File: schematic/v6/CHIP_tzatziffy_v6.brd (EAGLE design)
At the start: 40.9 x 49.8 mm, 51 parts, among them J1 2X20-CHIP0.8_DRILL, J3 S2B-PH-SM4-TB, Q1 NPN-DTC114YUA, Q2 PNP-DTA114YUA, U1 LMR62421, U3 DS2431P, X1 FH12-40S-0.5SH

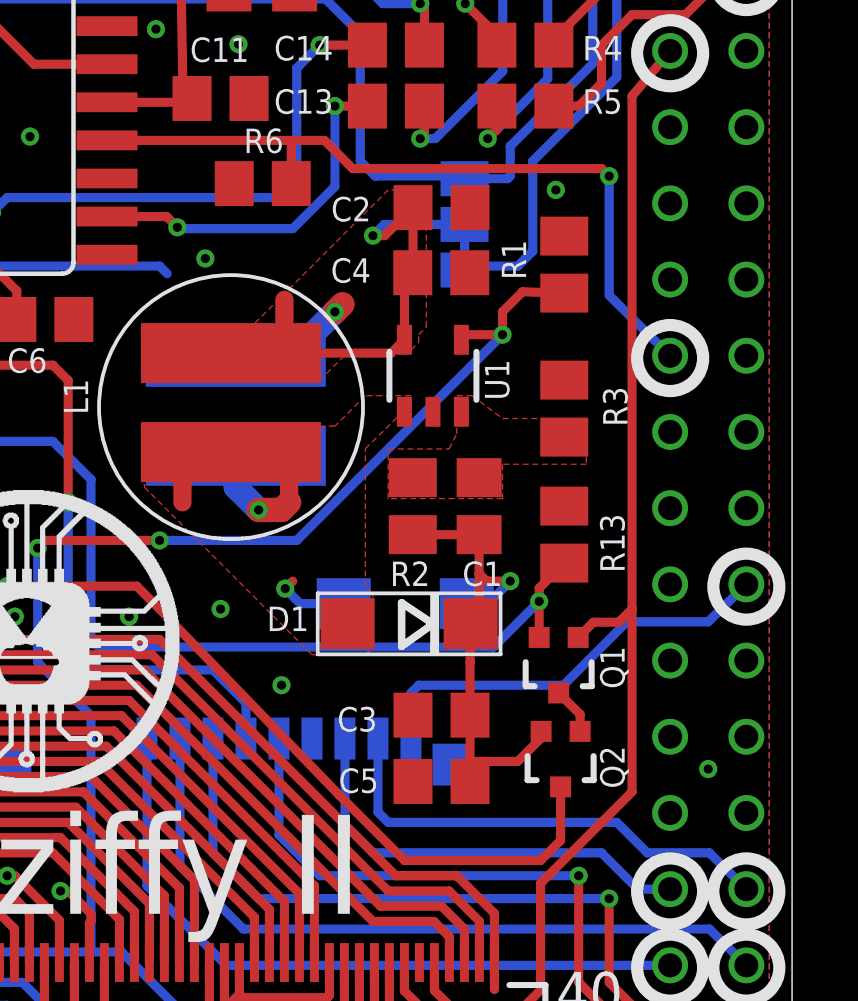
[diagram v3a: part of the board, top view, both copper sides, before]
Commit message: changed 22uF Footprint to 1206
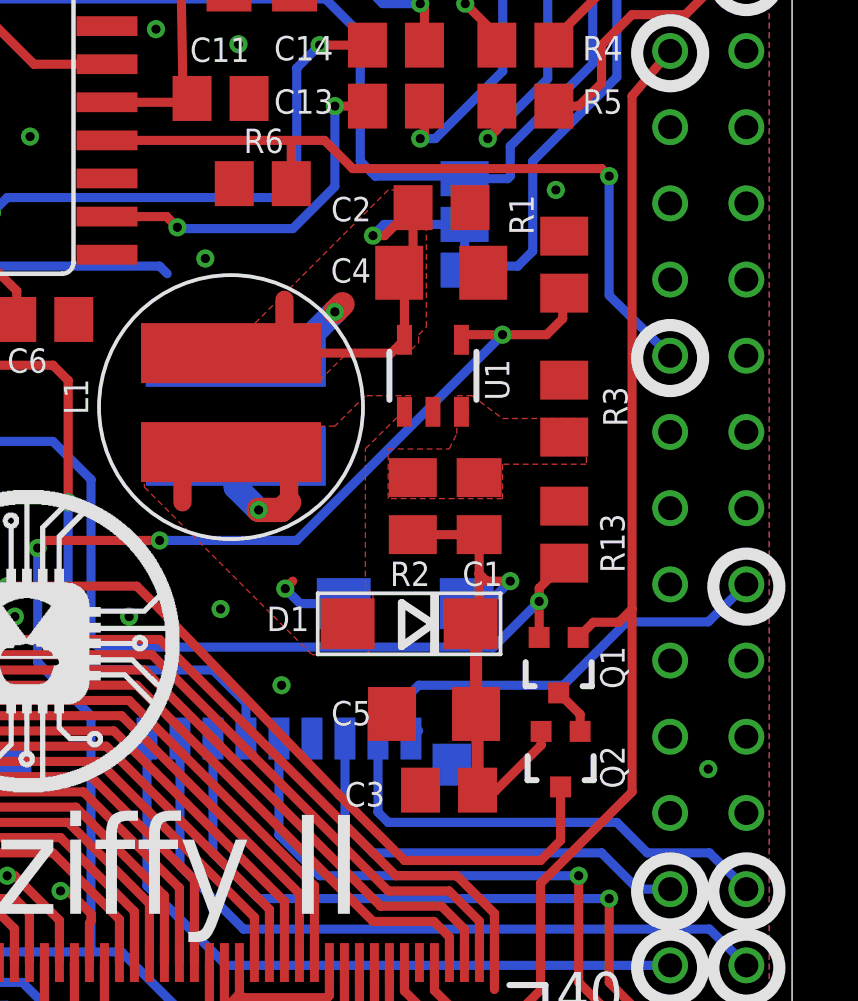
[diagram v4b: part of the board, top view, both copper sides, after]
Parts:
- C4, C5: device rcl:C0805 -> rcl:C1206
- moved C3 2.51 mm to (29.5, 14.3)
- moved C5 2.26 mm to (29.0, 16.8)
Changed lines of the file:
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@@
 </element>
 <element name="R1" library="rcl" package="M0805" value="100K" x="33.3" y="31.8" smashed="yes" rot="R90">
-<attribute name="NAME" x="32.03" y="31.292" size="0.8128" layer="25" rot="R90"/>
+<attribute name="NAME" x="32.28" y="32.792" size="0.8128" layer="25" rot="R90"/>
 <attribute name="VALUE" x="35.84" y="30.53" size="1.27" layer="27" rot="R90"/>
 </element>
@@
 <attribute name="NAME" x="25.527" y="33.2428" size="0.8128" layer="25" font="vector" ratio="12"/>
 </element>
-<element name="C3" library="rcl" package="C0805" value="100nF" x="29.21" y="16.7818" smashed="yes" rot="R180">
-<attribute name="NAME" x="25.7302" y="16.2382" size="0.8128" layer="25" font="vector" ratio="12"/>
-</element>
-<element name="C4" library="rcl" package="C0805" value="22uF" x="29.2" y="31.529" smashed="yes">
+<element name="C3" library="rcl" package="C0805" value="100nF" x="29.46" y="14.2818" smashed="yes" rot="R180">
+<attribute name="NAME" x="25.9802" y="13.7382" size="0.8128" layer="25" font="vector" ratio="12"/>
+</element>
+<element name="C4" library="rcl" package="C1206" value="22uF" x="29.2" y="31.529" smashed="yes">
 <attribute name="NAME" x="25.517" y="31.1988" size="0.8128" layer="25" font="vector" ratio="12"/>
 </element>
-<element name="C5" library="rcl" package="C0805" value="22uF" x="29.21" y="14.572" smashed="yes" rot="R180">
-<attribute name="NAME" x="25.781" y="14.191" size="0.8128" layer="25" font="vector" ratio="12"/>
+<element name="C5" library="rcl" package="C1206" value="22uF" x="28.96" y="16.822" smashed="yes" rot="R180">
+<attribute name="NAME" x="25.531" y="16.441" size="0.8128" layer="25" font="vector" ratio="12"/>
 </element>
 <element name="L1" library="Keyboard v0_5" package="SRN6045" value="SRN6045-100M" x="22.192" y="27.051" smashed="yes" rot="R270">
@@
 <contactref element="D1" pad="C"/>
 <contactref element="Q2" pad="2"/>
-<wire x1="30.16" y1="14.572" x2="30.16" y2="16.7818" width="0.3048" layer="1"/>
-<wire x1="30.16" y1="16.7818" x2="30.16" y2="18.5364" width="0.3048" layer="1"/>
-<wire x1="30.16" y1="18.5364" x2="30.1796" y2="19.826" width="0.3048" layer="1"/>
 <wire x1="29.718" y1="20.2768" x2="29.718" y2="19.558" width="0.3048" layer="1"/>
 <wire x1="29.718" y1="19.558" x2="29.986" y2="19.826" width="0.3048" layer="1"/>
 <wire x1="29.986" y1="19.826" x2="30.1796" y2="19.826" width="0.3048" layer="1"/>
-<wire x1="32.528496875" y1="16.2404625" x2="32.528496875" y2="16.018496875" width="0.3048" layer="1"/>
-<wire x1="32.528496875" y1="16.018496875" x2="31.75" y2="15.24" width="0.3048" layer="1"/>
-<wire x1="31.75" y1="15.24" x2="30.254" y2="15.24" width="0.3048" layer="1"/>
-<wire x1="30.254" y1="15.24" x2="30.16" y2="14.572" width="0.3048" layer="1"/>
 <wire x1="28.2524" y1="22.799" x2="30.4622" y2="22.799" width="0.3048" layer="1"/>
 <wire x1="30.1796" y1="19.826" x2="30.4622" y2="20.1086" width="0.3048" layer="1"/>
@@
 <wire x1="31.5" y1="21.25" x2="30.7122" y2="21.25" width="0.3048" layer="1"/>
 <wire x1="30.7122" y1="21.25" x2="30.4622" y2="21.5" width="0.3048" layer="1"/>
+<wire x1="30.1796" y1="19.826" x2="30.36" y2="19.826" width="0.4064" layer="1"/>
+<wire x1="30.36" y1="19.826" x2="30.36" y2="16.822" width="0.4064" layer="1"/>
+<wire x1="30.36" y1="16.822" x2="30.41" y2="16.822" width="0.4064" layer="1"/>
+<wire x1="30.41" y1="16.822" x2="30.41" y2="14.2818" width="0.4064" layer="1"/>
+<wire x1="32.528496875" y1="16.2404625" x2="32.528496875" y2="15.778496875" width="0.3048" layer="1"/>
+<wire x1="32.528496875" y1="15.778496875" x2="31" y2="14.25" width="0.3048" layer="1"/>
+<wire x1="31" y1="14.25" x2="30.4418" y2="14.25" width="0.3048" layer="1"/>
+<wire x1="30.4418" y1="14.25" x2="30.41" y2="14.2818" width="0.3048" layer="1"/>
 </signal>
 <signal name="FB">
@@
 <wire x1="22.192" y1="28.851" x2="27.53" y2="28.851" width="0.3048" layer="1"/>
 <wire x1="27.53" y1="28.851" x2="27.973" y2="29.294" width="0.3048" layer="1"/>
-<wire x1="28.25" y1="31.529" x2="28.26" y2="31.5798" width="0.3048" layer="1"/>
-<wire x1="28.25" y1="31.529" x2="27.973" y2="31.2928" width="0.3048" layer="1"/>
+<wire x1="27.8" y1="31.529" x2="28.26" y2="31.5798" width="0.3048" layer="1"/>
+<wire x1="27.8" y1="31.529" x2="27.973" y2="31.2928" width="0.3048" layer="1"/>
 <wire x1="27.973" y1="31.2928" x2="27.973" y2="29.294" width="0.3048" layer="1"/>
 <via x="26.924" y="32.766" extent="1-16" drill="0.3048"/>
@@
 <wire x1="24.384" y1="22.606" x2="19.812" y2="22.606" width="0.3048" layer="16"/>
 <wire x1="31.336" y1="29.37" x2="31.242" y2="29.464" width="0.3048" layer="1"/>
-<wire x1="31.242" y1="29.464" x2="31.242" y2="30.226" width="0.3048" layer="1"/>
-<wire x1="31.242" y1="30.226" x2="31.91" y2="30.894" width="0.3048" layer="1"/>
-<wire x1="31.91" y1="30.894" x2="33.3" y2="30.85" width="0.3048" layer="1"/>
 <wire x1="17.526" y1="8.89" x2="18.542" y2="8.89" width="0.3048" layer="16"/>
 <wire x1="18.542" y1="8.89" x2="21.844" y2="5.588" width="0.3048" layer="16"/>
@@
 <wire x1="23.876" y1="6.35" x2="21.844" y2="4.318" width="0.3048" layer="1"/>
 <wire x1="21.844" y1="4.318" x2="21.844" y2="3.81" width="0.3048" layer="1"/>
+<wire x1="31.242" y1="29.464" x2="32.714" y2="29.464" width="0.3048" layer="1"/>
+<wire x1="32.714" y1="29.464" x2="33.25" y2="30" width="0.3048" layer="1"/>
+<wire x1="33.25" y1="30" x2="33.25" y2="30.8" width="0.3048" layer="1"/>
+<wire x1="33.25" y1="30.8" x2="33.3" y2="30.85" width="0.3048" layer="1"/>
 </signal>
 <signal name="VCC-1V8">
